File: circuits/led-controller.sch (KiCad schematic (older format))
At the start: 13 parts, among them J1 Conn_02x02_Odd_Even, P1 CONN_01X03, SW1 Rotary_Encoder_Switch, U1? REG-3.3v, U2 PIR-DIGITAL

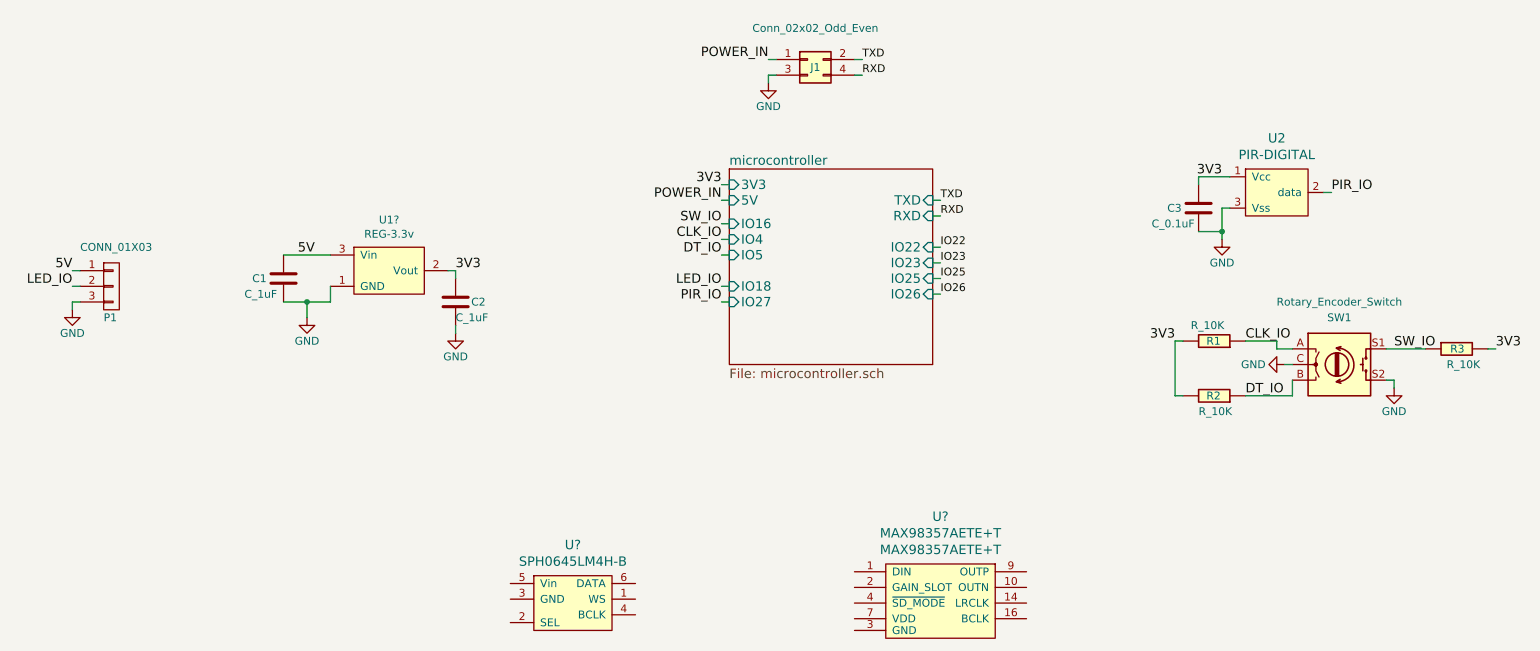
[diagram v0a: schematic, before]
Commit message: sending new board to boardhouse
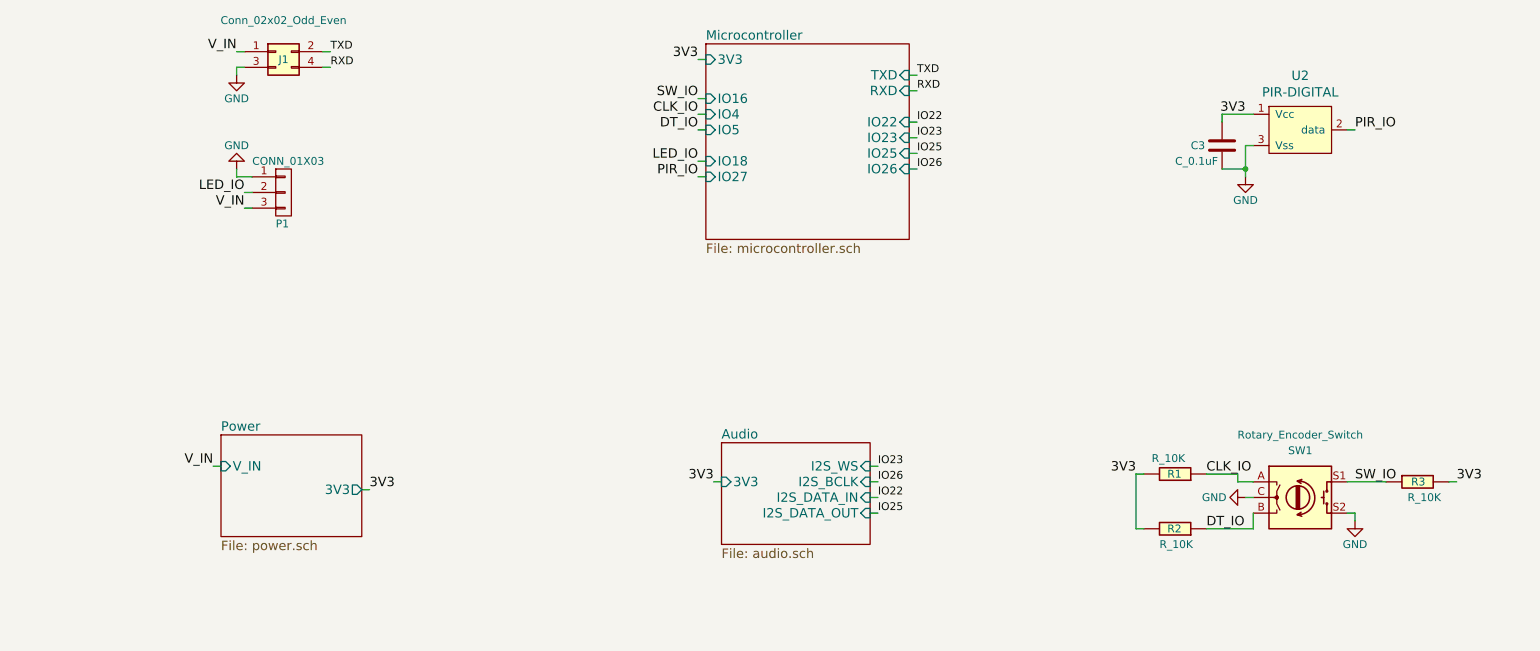
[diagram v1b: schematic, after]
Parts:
- removed C1, C2: C_1uF, Capacitor_SMD:C_0603_1608Metric_Pad1.05x0.95mm_HandSolder, symbol led-controller-rescue:C_1uF-open-automation
- removed U1?: REG-3.3v, Package_TO_SOT_SMD:TO-252-2, symbol open-automation:REG-3.3v
- removed U?: SPH0645LM4H-B, open-automation:SPH0645LM4H-B, symbol open-automation:SPH0645LM4H-B
- removed U?: MAX98357AETE+T, open-automation:MAX98357A, symbol open-automation:MAX98357AETE+T
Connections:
- net 5V is gone; now on net GND: P1.1 (P1)
- net GND: no longer P1.3 (P3)
- net POWER_IN renamed V_IN
- net V_IN: now also P1.3 (P3)
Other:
- moved on the sheet: C3, J1, P1, R1, R2, R3, SW1, U2
